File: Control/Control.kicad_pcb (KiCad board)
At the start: 2 copper layers, 144.8 x 73.9 mm, 60 parts, among them J1 Conn_01x04_Pin, J2 Conn_01x08_Pin, J3 Conn_01x08_Pin, J4 Conn_01x07_Pin, SW1 SW_MEC_5E, U1 AT28C64B-15PI, U2 AT28C64B-15PI, U3 SN74AC14N, U4 SN74AC14N, U5 74LS163, U6 74HCT138, U7 74HCT00

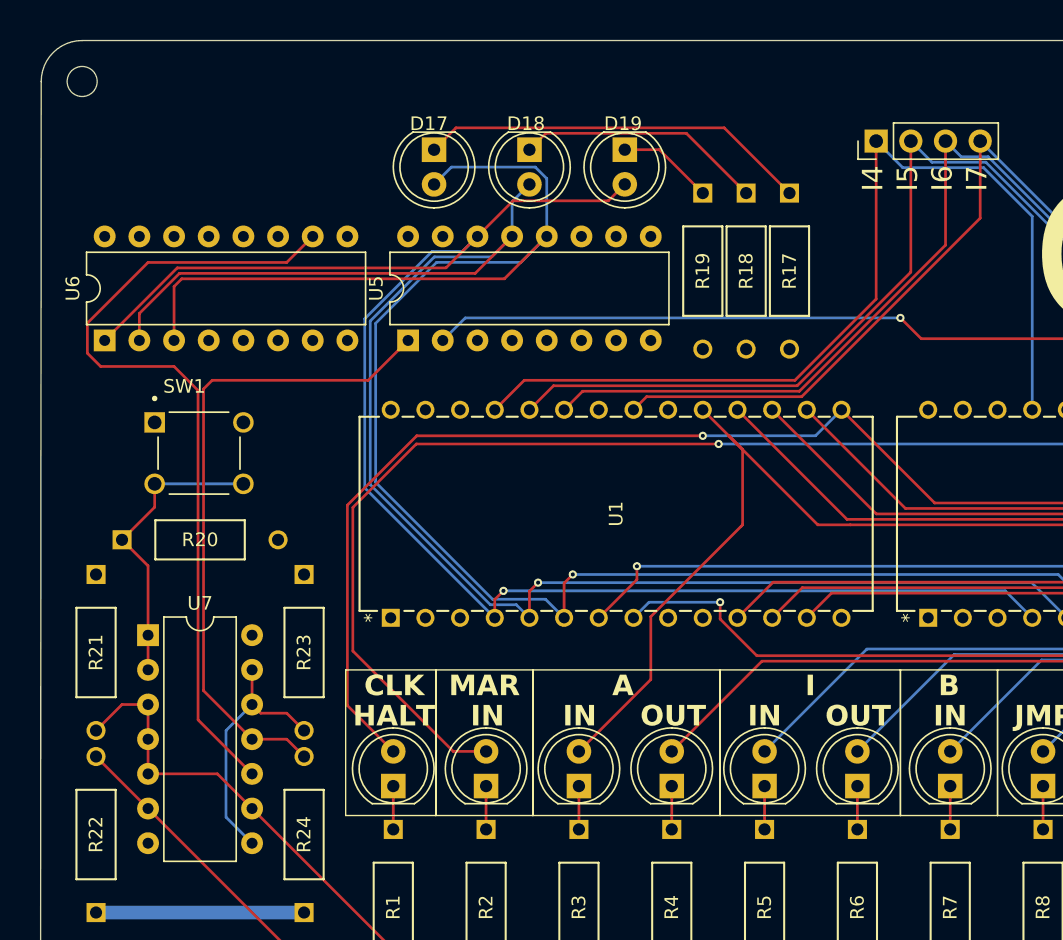
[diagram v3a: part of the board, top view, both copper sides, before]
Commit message: Updated microcode timer LEDs to 1 hot signal instead of binary counter
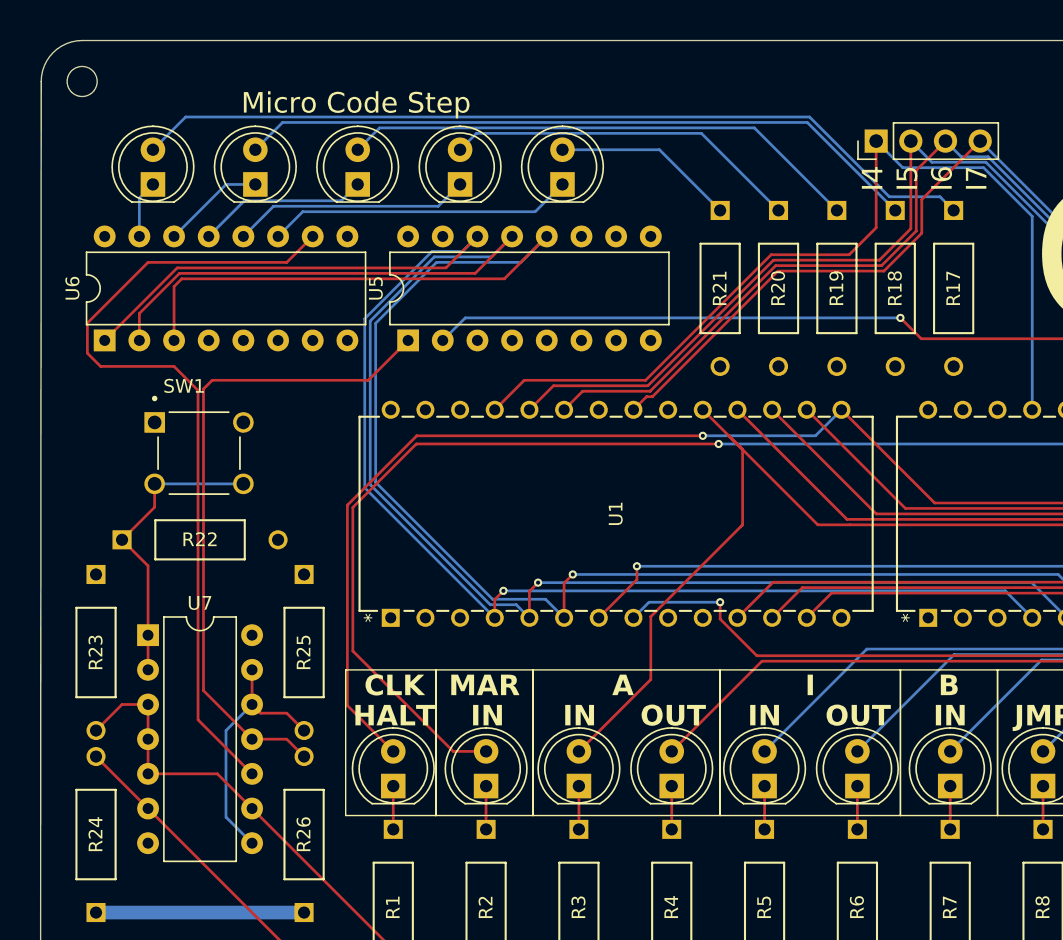
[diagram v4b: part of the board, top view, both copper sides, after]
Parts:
- added D20: LED, LED_THT:LED_D5.0mm, F.Cu at (85.1, 88.3)
- added D21: LED, LED_THT:LED_D5.0mm, F.Cu at (92.6, 88.3)
- added R20: 1k, _DownloadFootprints:CF_series_Resistors_THT, F.Cu at (108.4, 90.2)
- added R21: 1k, _DownloadFootprints:CF_series_Resistors_THT, F.Cu at (104.1, 90.2)
- moved D17 20.8 mm to (62.6, 88.3), turned to 90 degrees
- moved D18 20.2 mm to (70.1, 88.3), turned to 90 degrees
- moved D19 19.7 mm to (77.6, 88.3), turned to 90 degrees
- moved R17 12.1 mm to (121.2, 90.2)
- moved R18 11.0 mm to (117.0, 90.2)
- moved R19 9.90 mm to (112.7, 90.2)
- renumbered R20 to R22, R21 to R23, R22 to R24, R23 to R25, R24 to R26
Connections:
- D17 pad 2: /T2 -> Net-(D17-A)
- D18 pad 2: /T1 -> Net-(D18-A)
- D19 pad 2: /T0 -> Net-(D19-A)
- R17 pad 1: Net-(D17-K) -> Net-(D17-A)
- R17 pad 2: GND -> +5V
- R18 pad 1: Net-(D18-K) -> Net-(D18-A)
- R18 pad 2: GND -> +5V
- R19 pad 1: Net-(D19-K) -> Net-(D19-A)
- R19 pad 2: GND -> +5V
- U6 pad 11: unconnected-(U6-~{Y4}-Pad11) -> Net-(D21-K)
- U6 pad 12: unconnected-(U6-~{Y3}-Pad12) -> Net-(D20-K)
- U6 pad 13: unconnected-(U6-~{Y2}-Pad13) -> Net-(D19-K)
- U6 pad 14: unconnected-(U6-~{Y1}-Pad14) -> Net-(D18-K)
- U6 pad 15: unconnected-(U6-~{Y0}-Pad15) -> Net-(D17-K)
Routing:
- net Net-(D17-A): track 0.00 -> 62.5 mm
- net Net-(D18-A): track 0.00 -> 50.4 mm
- net Net-(D19-A): track 0.00 -> 38.3 mm
- net Net-(D20-A): track 0.00 -> 26.2 mm
- net Net-(D17-K): track 28.7 -> 4.22 mm
- net Net-(D21-K): track 0.00 -> 22.4 mm
- net Net-(D20-K): track 0.00 -> 17.5 mm
- net Net-(D21-A): track 0.00 -> 13.4 mm
- net /T2: track 134.4 -> 121.0 mm
- net /T0: track 121.2 -> 108.9 mm
- net Net-(D18-K): track 18.2 -> 7.53 mm
- net Net-(D19-K): track 7.03 -> 12.5 mm
- net /T1: track 119.2 -> 114.9 mm
- net /IR4: track 70.8 -> 67.7 mm
- net /IR6: track 66.1 -> 64.3 mm
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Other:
- board text added: "Micro Code Step"

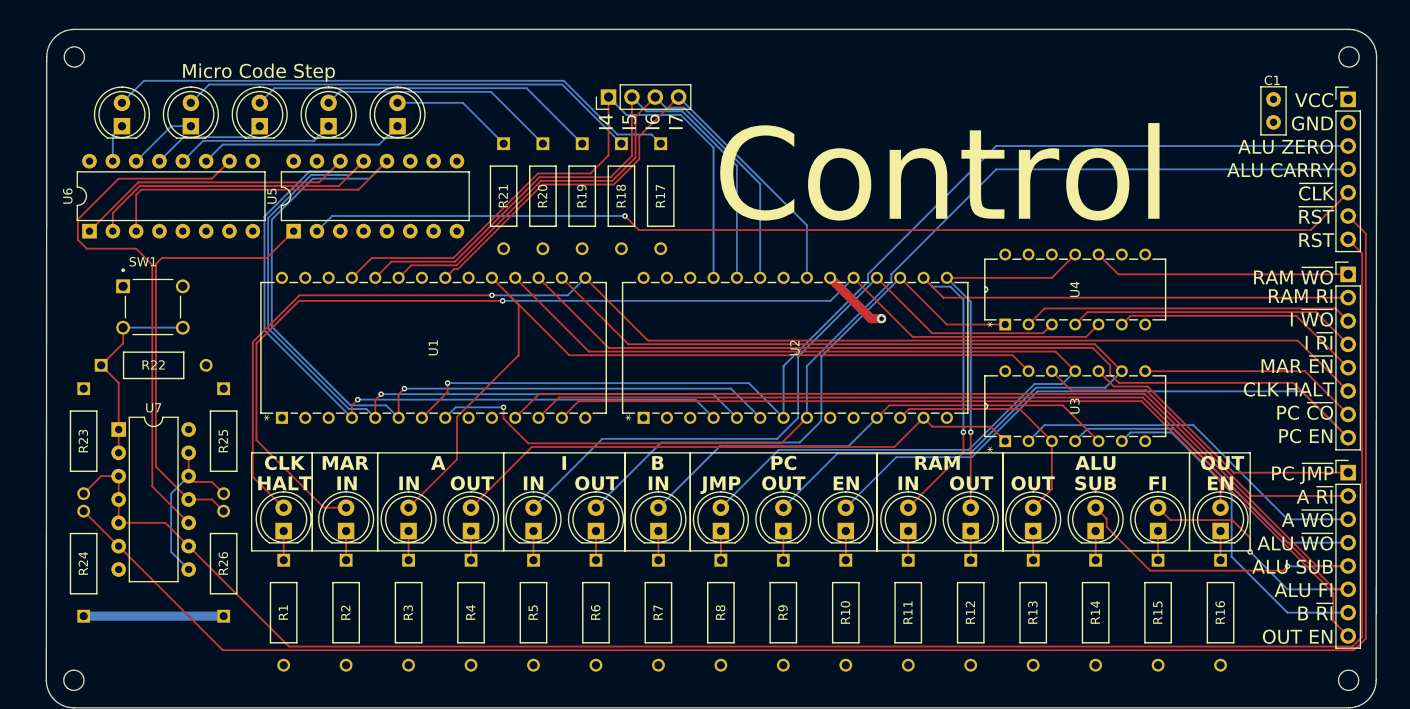
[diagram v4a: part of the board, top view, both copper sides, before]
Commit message: Added spare pins to control
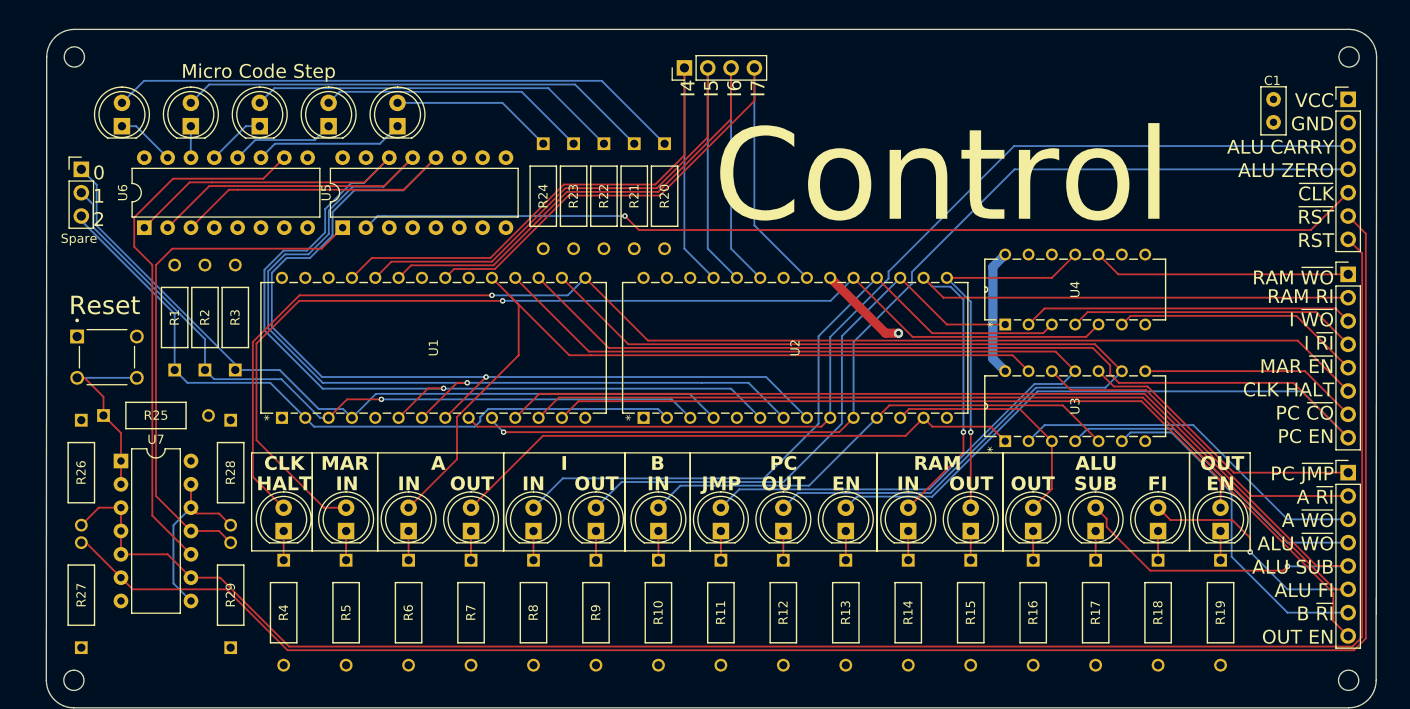
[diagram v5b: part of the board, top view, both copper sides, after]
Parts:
- added J1: Conn_01x03_Pin, Connector_PinHeader_2.54mm:PinHeader_1x03_P2.54mm_Vertical, F.Cu at (58.2, 93.0)
- added R1: 1k, _DownloadFootprints:CF_series_Resistors_THT, F.Cu at (68.3, 114.8)
- added R2: 1k, _DownloadFootprints:CF_series_Resistors_THT, F.Cu at (71.6, 114.8)
- added R3: 1k, _DownloadFootprints:CF_series_Resistors_THT, F.Cu at (74.9, 114.8)
- moved J2 8.84 mm to (123.8, 81.9)
- moved SW1 7.41 mm to (61.0, 113.4)
- moved U6 5.98 mm to (65.0, 99.3)
- moved R25 5.47 mm to (60.6, 119.8)
- moved U5 5.35 mm to (86.6, 99.3)
- moved R24 4.32 mm to (108.5, 90.2)
- moved R28 3.51 mm to (74.4, 120.3)
- moved R29 3.51 mm to (74.4, 145.0)
- moved R26 3.44 mm to (58.2, 120.3)
- moved R27 3.44 mm to (58.2, 145.0)
- moved U7 3.44 mm to (62.5, 124.7)
- moved R23 3.34 mm to (111.8, 90.2)
- moved R22 2.37 mm to (115.1, 90.2)
- moved R21 1.39 mm to (118.4, 90.2)
- moved R20 0.42 mm to (121.7, 90.2)
- renumbered J1 to J2, J2 to J3, J3 to J4, J4 to J5, R7 to R10, R8 to R11, R9 to R12, R10 to R13, R11 to R14, R12 to R15, R13 to R16, R14 to R17, R15 to R18, R16 to R19, R17 to R20, R18 to R21, R19 to R22, R20 to R23, R21 to R24, R22 to R25, R23 to R26, R24 to R27, R25 to R28, R26 to R29, R1 to R4, R2 to R5, R3 to R6, R4 to R7, R5 to R8, R6 to R9
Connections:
- J5 pad 3: /ALU_ZERO -> /ALU_CARRY
- J5 pad 4: /ALU_CARRY -> /ALU_ZERO
- U1 pad 10: +5V -> /ALU_ZERO
- U1 pad 2: GND -> /Spare2
- U1 pad 3: GND -> /Spare1
- U1 pad 4: /T0 -> /Spare0
- U1 pad 5: /T1 -> +5V
- U1 pad 6: /T2 -> /T0
- U1 pad 7: /ALU_ZERO -> /T1
- U1 pad 8: /ALU_CARRY -> /T2
- U1 pad 9: GND -> /ALU_CARRY
- U2 pad 10: GND -> /ALU_ZERO
- U2 pad 2: GND -> /Spare2
- U2 pad 3: GND -> /Spare1
- U2 pad 4: /T0 -> /Spare0
- U2 pad 5: /T1 -> GND
- U2 pad 6: /T2 -> /T0
- U2 pad 7: /ALU_ZERO -> /T1
- U2 pad 8: /ALU_CARRY -> /T2
- U2 pad 9: GND -> /ALU_CARRY
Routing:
- net /Spare0: track 0.00 -> 85.2 mm
- net /Spare1: track 0.00 -> 81.5 mm, vias 0 -> 1
- net /Spare2: track 0.00 -> 78.6 mm
- net /T0: track 108.9 -> 120.8 mm
- net /T1: track 114.9 -> 125.0 mm
- net /IR7: track 60.5 -> 70.5 mm
- net /MicroCodeTimer/~{RST}: track 47.9 -> 57.4 mm
- net /ALU_ZERO: track 120.6 -> 111.5 mm
- net /IR6: track 64.3 -> 73.1 mm
- net /T2: track 121.0 -> 128.9 mm
- net /IR4: track 67.7 -> 75.4 mm
- net /IR5: track 66.6 -> 74.3 mm
- net Net-(D21-K): track 22.4 -> 16.3 mm
- net Net-(D19-K): track 12.5 -> 6.37 mm
- net Net-(D20-K): track 17.5 -> 11.3 mm
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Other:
- board text added: "0"
- board text added: "1"
- board text added: "2"
- board text added: "Reset"
- board text added: "Spare"

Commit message: Final silkscreen updates
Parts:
- moved D17 0.38 mm to (62.6, 87.9)
- moved D18 0.38 mm to (70.1, 87.9)
- moved D19 0.38 mm to (77.6, 87.9)
- moved D20 0.38 mm to (85.1, 87.9)
- moved D21 0.38 mm to (92.6, 87.9)
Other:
- board text added: "Inverter"
- board text added: "Micro code timer"
- board text added: "Reset Logic"
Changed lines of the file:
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@@
 	(footprint "LED_THT:LED_D5.0mm"
 		(layer "F.Cu")
-		(at 70.09 88.265 90)
+		(at 70.09 87.884 90)
 		(descr "LED, diameter 5.0mm, 2 pins, http://cdn-reichelt.de/documents/datenblatt/A500/LL-504BC2E-009.pdf")
 		(tags "LED diameter 5.0mm 2 pins")
@@
 		)
 		(fp_text user "*"
-			(at -8.514 -16.6497 90)
+			(at -8.255 -16.6497 90)
 			(unlocked yes)
 			(layer "F.SilkS")
@@
 	(footprint "LED_THT:LED_D5.0mm"
 		(layer "F.Cu")
-		(at 62.59 88.265 90)
+		(at 62.59 87.884 90)
 		(descr "LED, diameter 5.0mm, 2 pins, http://cdn-reichelt.de/documents/datenblatt/A500/LL-504BC2E-009.pdf")
 		(tags "LED diameter 5.0mm 2 pins")
@@
 		(tags "THT DIP DIL PDIP 2.54mm 7.62mm 300mil")
 		(property "Reference" "U6"
-			(at 3.81 -2.33 90)
+			(at 3.81 -2.54 90)
 			(layer "F.SilkS")
 			(effects
@@
 	(footprint "LED_THT:LED_D5.0mm"
 		(layer "F.Cu")
-		(at 92.59 88.265 90)
+		(at 92.59 87.884 90)
 		(descr "LED, diameter 5.0mm, 2 pins, http://cdn-reichelt.de/documents/datenblatt/A500/LL-504BC2E-009.pdf")
 		(tags "LED diameter 5.0mm 2 pins")
@@
 	(footprint "LED_THT:LED_D5.0mm"
 		(layer "F.Cu")
-		(at 85.09 88.265 90)
+		(at 85.09 87.884 90)
 		(descr "LED, diameter 5.0mm, 2 pins, http://cdn-reichelt.de/documents/datenblatt/A500/LL-504BC2E-009.pdf")
 		(tags "LED diameter 5.0mm 2 pins")
@@
 	(footprint "LED_THT:LED_D5.0mm"
 		(layer "F.Cu")
-		(at 77.59 88.265 90)
+		(at 77.59 87.884 90)
 		(descr "LED, diameter 5.0mm, 2 pins, http://cdn-reichelt.de/documents/datenblatt/A500/LL-504BC2E-009.pdf")
 		(tags "LED diameter 5.0mm 2 pins")
@@
 	)
 	(gr_rect
+		(start 155.956 101.092)
+		(end 176.784 123.698)
+		(stroke
+			(width 0.1)
+			(type default)
+		)
+		(fill none)
+		(layer "F.SilkS")
+	)
+	(gr_rect
 		(start 104.14 123.83)
 		(end 117.348 134.498)
@@
 		(layer "F.SilkS")
 	)
+	(gr_line
+		(start 106.172 90.424)
+		(end 106.172 100.584)
+		(stroke
+			(width 0.1)
+			(type default)
+		)
+		(layer "F.SilkS")
+	)
 	(gr_rect
 		(start 83.312 123.83)
@@
 		(layer "F.SilkS")
 	)
+	(gr_line
+		(start 106.172 100.584)
+		(end 63.246 100.584)
+		(stroke
+			(width 0.1)
+			(type default)
+		)
+		(layer "F.SilkS")
+	)
 	(gr_rect
 		(start 117.348 123.83)
@@
 	)
 	(gr_rect
+		(start 56.388 118.11)
+		(end 76.2 146.304)
+		(stroke
+			(width 0.1)
+			(type default)
+		)
+		(fill none)
+		(layer "F.SilkS")
+	)
+	(gr_line
+		(start 63.246 90.424)
+		(end 106.172 90.424)
+		(stroke
+			(width 0.1)
+			(type default)
+		)
+		(layer "F.SilkS")
+	)
+	(gr_rect
 		(start 178.816 123.83)
 		(end 185.42 134.498)
@@
 	)
 	(gr_line
+		(start 63.246 100.584)
+		(end 63.246 90.424)
+		(stroke
+			(width 0.1)
+			(type default)
+		)
+		(layer "F.SilkS")
+	)
+	(gr_line
 		(start 196.136 151.59)
 		(end 57.356 151.59)
@@
 		)
 	)
+	(gr_text "Reset Logic"
+		(at 56.388 118.11 0)
+		(layer "F.SilkS")
+		(effects
+			(font
+				(size 1 1)
+				(thickness 0.1)
+			)
+			(justify left bottom)
+		)
+	)
 	(gr_text "SUB"
 		(at 168.595462 128.079 0)
@@
 		)
 	)
+	(gr_text "Micro code timer"
+		(at 63.246 90.424 0)
+		(layer "F.SilkS")
+		(effects
+			(font
+				(size 1 1)
+				(thickness 0.1)
+			)
+			(justify left bottom)
+		)
+	)
 	(gr_text "GND"
 		(at 194.564 88.9 0)
@@
 		)
 	)
+	(gr_text "Inverter"
+		(at 155.956 101.092 0)
+		(layer "F.SilkS")
+		(effects
+			(font
+				(size 1 1)
+				(thickness 0.1)
+			)
+			(justify left bottom)
+		)
+	)
 	(gr_text "OUT"
 		(at 114.245924 128.079 0)
@@
 	)
 	(segment
-		(start 62.59 88.265)
-		(end 64.135 88.265)
+		(start 62.59 87.884)
+		(end 63.754 87.884)
 		(width 0.2)
 		(layer "B.Cu")
@@
 	)
 	(segment
-		(start 64.135 88.265)
+		(start 63.754 87.884)
 		(end 67.564 91.694)
 		(width 0.2)
@@
 	)
 	(segment
-		(start 70.09 91.68)
-		(end 70.104 91.694)
+		(start 70.09 87.884)
+		(end 70.09 91.68)
 		(width 0.2)
 		(layer "B.Cu")
@@
 	)
 	(segment
-		(start 70.09 88.265)
-		(end 70.09 91.68)
+		(start 70.09 91.68)
+		(end 70.104 91.694)
 		(width 0.2)
 		(layer "B.Cu")
@@
 	)
 	(segment
-		(start 76.073 88.265)
+		(start 76.454 87.884)
 		(end 72.644 91.694)
 		(width 0.2)
@@
 	)
 	(segment
-		(start 77.59 88.265)
-		(end 76.073 88.265)
+		(start 77.59 87.884)
+		(end 76.454 87.884)
 		(width 0.2)
 		(layer "B.Cu")
@@
 	)
 	(segment
-		(start 64.99 83.325)
-		(end 114.821 83.325)
+		(start 114.116 82.62)
+		(end 121.666 90.17)
 		(width 0.2)
 		(layer "B.Cu")
@@
 	)
 	(segment
-		(start 62.59 85.725)
-		(end 64.99 83.325)
+		(start 65.314 82.62)
+		(end 114.116 82.62)
 		(width 0.2)
 		(layer "B.Cu")
@@
 	)
 	(segment
-		(start 114.821 83.325)
-		(end 121.666 90.17)
+		(start 62.59 85.344)
+		(end 65.314 82.62)
 		(width 0.2)
 		(layer "B.Cu")
@@
 	)
 	(segment
-		(start 111.919 83.725)
-		(end 118.364 90.17)
+		(start 70.09 85.344)
+		(end 72.414 83.02)
 		(width 0.2)
 		(layer "B.Cu")
@@
 	)
 	(segment
-		(start 72.09 83.725)
-		(end 111.919 83.725)
+		(start 72.414 83.02)
+		(end 110.3155 83.02)
 		(width 0.2)
 		(layer "B.Cu")
@@
 	)
 	(segment
-		(start 70.09 85.725)
-		(end 72.09 83.725)
+		(start 110.3155 83.02)
+		(end 117.4655 90.17)
 		(width 0.2)
 		(layer "B.Cu")
@@
 	)
 	(segment
-		(start 109.017 84.125)
+		(start 117.4655 90.17)
+		(end 118.364 90.17)
+		(width 0.2)
+		(layer "B.Cu")
+		(net 73)
+	)
+	(segment
+		(start 114.1635 90.17)
 		(end 115.062 90.17)
 		(width 0.2)
@@
 	)
 	(segment
-		(start 77.59 85.725)
-		(end 79.19 84.125)
+		(start 77.59 85.344)
+		(end 79.514 83.42)
 		(width 0.2)
 		(layer "B.Cu")
@@
 	)
 	(segment
-		(start 79.19 84.125)
-		(end 109.017 84.125)
+		(start 107.4135 83.42)
+		(end 114.1635 90.17)
 		(width 0.2)
 		(layer "B.Cu")
@@
 	)
 	(segment
-		(start 77.108 89.77)
-		(end 75.184 91.694)
+		(start 79.514 83.42)
+		(end 107.4135 83.42)
 		(width 0.2)
 		(layer "B.Cu")
-		(net 75)
+		(net 74)
 	)
 	(segment
-		(start 83.585 89.77)
+		(start 83.204 89.77)
 		(end 77.108 89.77)
 		(width 0.2)
@@
 	)
 	(segment
-		(start 85.09 88.265)
-		(end 83.585 89.77)
+		(start 77.108 89.77)
+		(end 75.184 91.694)
 		(width 0.2)
 		(layer "B.Cu")
@@
 	)
 	(segment
-		(start 85.09 85.725)
-		(end 86.29 84.525)
+		(start 85.09 87.884)
+		(end 83.204 89.77)
 		(width 0.2)
 		(layer "B.Cu")
-		(net 77)
+		(net 75)
 	)
 	(segment
-		(start 86.29 84.525)
-		(end 106.115 84.525)
+		(start 86.614 83.82)
+		(end 105.41 83.82)
 		(width 0.2)
 		(layer "B.Cu")
@@
 	)
 	(segment
-		(start 106.115 84.525)
+		(start 105.41 83.82)
 		(end 111.76 90.17)
 		(width 0.2)
@@
 	)
 	(segment
+		(start 85.09 85.344)
+		(end 86.614 83.82)
+		(width 0.2)
+		(layer "B.Cu")
+		(net 77)
+	)
+	(segment
 		(start 68.158 93.98)
 		(end 77.978 93.98)
@@
 	)
 	(segment
-		(start 90.685 90.17)
+		(start 90.304 90.17)
 		(end 79.248 90.17)
 		(width 0.2)
@@
 	)
 	(segment
-		(start 92.59 88.265)
-		(end 90.685 90.17)
+		(start 92.59 87.884)
+		(end 90.304 90.17)
 		(width 0.2)
 		(layer "B.Cu")
@@
 	)
 	(segment
-		(start 92.59 85.725)
-		(end 104.013 85.725)
+		(start 104.013 85.725)
+		(end 108.458 90.17)
 		(width 0.2)
 		(layer "B.Cu")
@@
 	)
 	(segment
-		(start 104.013 85.725)
-		(end 108.458 90.17)
+		(start 92.59 85.344)
+		(end 92.971 85.725)
+		(width 0.2)
+		(layer "B.Cu")
+		(net 85)
+	)
+	(segment
+		(start 92.971 85.725)
+		(end 104.013 85.725)
 		(width 0.2)
 		(layer "B.Cu")
